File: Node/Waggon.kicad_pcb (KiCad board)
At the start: 2 copper layers, 34.3 x 74.9 mm, 40 parts, among them J1 Screw_Terminal_01x05, J10 Conn_01x01, J11 Conn_01x01, J12 Conn_01x01, J13 Conn_01x01, J14 Conn_01x01, J15 Conn_01x01, J16 Conn_01x01, J17 Conn_01x01, J18 Conn_01x01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

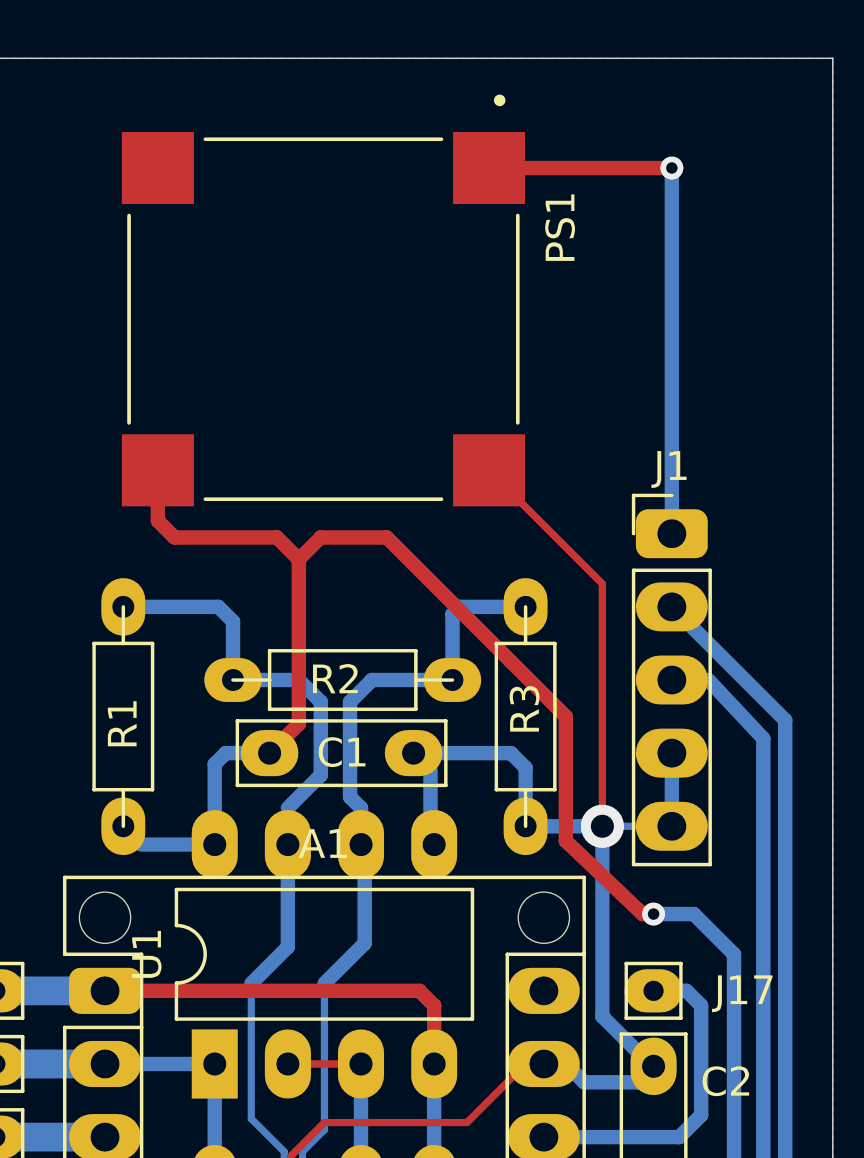
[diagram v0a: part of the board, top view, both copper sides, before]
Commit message: Adding KiCAD Footprints
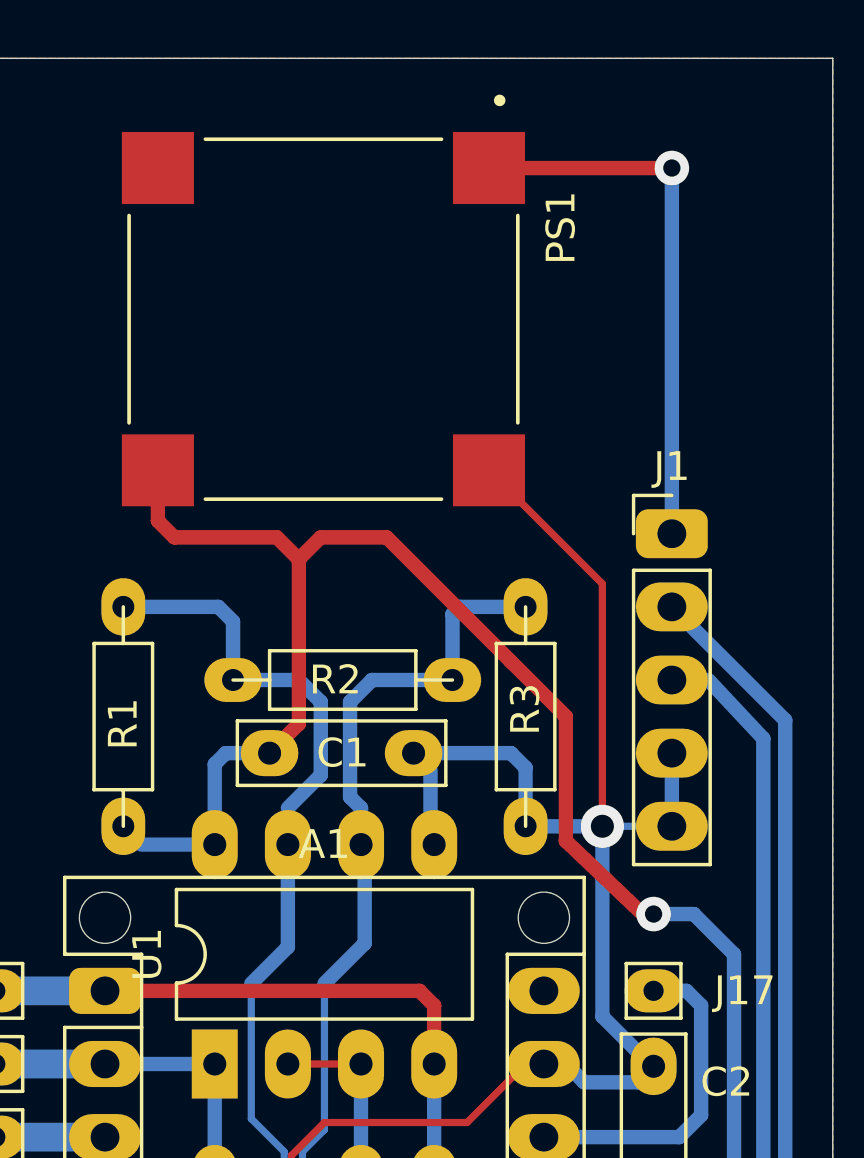
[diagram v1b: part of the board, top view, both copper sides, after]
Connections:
- A1 pad 30: Net-(A1-Pad30) -> unconnected-(A1-Pad30)
- PS1 pad 4: Net-(PS1-Pad4) -> unconnected-(PS1-Pad4)
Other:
- net class Default removed

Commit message: Updating Descriptions
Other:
- board text added: "+9..36V"
- board text added: "/RESET"
- board text added: "3V3"
- board text added: "A0"
- board text added: "A1"
- board text added: "A2"
- board text added: "A3"
- board text added: "A4"
- board text added: "A5"
- board text added: "A6"
- board text added: "A7"
- board text added: "ARef"
- board text added: "D10"
- board text added: "D13 / SCK / Built-In-LED"
- board text added: "D2"
- board text added: "D3"
- board text added: "D4"
- board text added: "D5"
- board text added: "D6"
- board text added: "D7"
- board text added: "D8"
- board text added: "D9"
- board text added: "GND"
- board text added: "LEDs in wagon DK: VU-Meter rt D2 ge D3 ge D4 gn D5 gn D7 gn D8 gn D9 gn D10 gn D13 LED top gn A7"
- board text added: "MISO / D12"
- board text added: "MOSI / D11"
- board text added: "PortA.0"
- board text added: "PortA.1"
- board text added: "PortA.2"
- board text added: "PortA.3"
- board text added: "PortA.4"
- board text added: "PortA.5"
- board text added: "PortA.6"
- board text added: "PortA.7"
- board text added: "PortB.0"
- board text added: "PortB.1"
- board text added: "PortB.2"
- board text added: "PortB.3"
- board text added: "PortB.4"
- board text added: "PortB.5"
- board text added: "PortB.6"
- board text added: "PortB.7"
- board text added: "RX1"
- board text added: "SCL / A"
- board text added: "SDA / B"
- board text added: "TX1"
- board text added: "black"
- board text added: "blue"
- board text added: "green"
- board text added: "magnetig connector"
- board text added: "plastic connector"
- board text added: "red"
- board text added: "white"
- board text added: "yellow"
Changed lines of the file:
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@@
   (gr_line (start 187.96 69.85) (end 222.25 69.85) (layer "Edge.Cuts") (width 0.05))
   (gr_line (start 222.25 144.78) (end 187.96 144.78) (layer "Edge.Cuts") (width 0.05))
+  (gr_text "/RESET" (at 226.314 102.108) (layer "F.SilkS")
+    (effects (font (size 1 1) (thickness 0.15)))
+  )
+  (gr_text "D10" (at 184.404 132.588) (layer "F.SilkS")
+    (effects (font (size 1 1) (thickness 0.15)))
+  )
+  (gr_text "D5" (at 185.039 119.888) (layer "F.SilkS")
+    (effects (font (size 1 1) (thickness 0.15)))
+  )
+  (gr_text "A5" (at 225.044 117.348) (layer "F.SilkS")
+    (effects (font (size 1 1) (thickness 0.15)))
+  )
+  (gr_text "A2" (at 225.044 124.968) (layer "F.SilkS")
+    (effects (font (size 1 1) (thickness 0.15)))
+  )
+  (gr_text "PortA.1" (at 177.419 114.808) (layer "F.SilkS")
+    (effects (font (size 1 1) (thickness 0.15)))
+  )
+  (gr_text "PortA.6" (at 177.419 127.508) (layer "F.SilkS")
+    (effects (font (size 1 1) (thickness 0.15)))
+  )
+  (gr_text "MISO / D12 " (at 181.864 137.668) (layer "F.SilkS")
+    (effects (font (size 1 1) (thickness 0.15)))
+  )
+  (gr_text "MOSI / D11" (at 181.229 135.128) (layer "F.SilkS")
+    (effects (font (size 1 1) (thickness 0.15)))
+  )
+  (gr_text "LEDs in wagon DK:\nVU-Meter\n	rt	D2\n	ge	D3\n	ge	D4\n	gn	D5\n	gn	D7\n	gn	D8\n	gn	D9\n	gn	D10\n	gn	D13\nLED top\n	gn	A7" (at 142.494 79.883) (layer "F.SilkS")
+    (effects (font (size 1 1) (thickness 0.15)) (justify left))
+  )
+  (gr_text "PortA.3" (at 177.419 119.888) (layer "F.SilkS")
+    (effects (font (size 1 1) (thickness 0.15)))
+  )
+  (gr_text "GND" (at 225.044 96.393) (layer "F.SilkS")
+    (effects (font (size 1 1) (thickness 0.15)))
+  )
+  (gr_text "ARef" (at 225.679 132.588) (layer "F.SilkS")
+    (effects (font (size 1 1) (thickness 0.15)))
+  )
+  (gr_text "D4" (at 185.039 117.348) (layer "F.SilkS")
+    (effects (font (size 1 1) (thickness 0.15)))
+  )
+  (gr_text "black" (at 248.539 93.853) (layer "F.SilkS")
+    (effects (font (size 1 1) (thickness 0.15)))
+  )
+  (gr_text "SCL / A" (at 226.314 91.313) (layer "F.SilkS")
+    (effects (font (size 1 1) (thickness 0.15)))
+  )
+  (gr_text "A0" (at 225.044 130.048) (layer "F.SilkS")
+    (effects (font (size 1 1) (thickness 0.15)))
+  )
+  (gr_text "D2" (at 185.039 112.268) (layer "F.SilkS")
+    (effects (font (size 1 1) (thickness 0.15)))
+  )
+  (gr_text "PortA.2" (at 177.419 117.348) (layer "F.SilkS")
+    (effects (font (size 1 1) (thickness 0.15)))
+  )
+  (gr_text "PortB.2" (at 171.069 137.668) (layer "F.SilkS")
+    (effects (font (size 1 1) (thickness 0.15)))
+  )
+  (gr_text "D13 / SCK / Built-In-LED" (at 234.569 137.668) (layer "F.SilkS")
+    (effects (font (size 1 1) (thickness 0.15)))
+  )
+  (gr_text "SDA / B" (at 226.314 88.773) (layer "F.SilkS")
+    (effects (font (size 1 1) (thickness 0.15)))
+  )
+  (gr_text "D8" (at 185.039 127.508) (layer "F.SilkS")
+    (effects (font (size 1 1) (thickness 0.15)))
+  )
+  (gr_text "plastic\nconnector" (at 246.634 81.788) (layer "F.SilkS")
+    (effects (font (size 1 1) (thickness 0.15)) (justify left))
+  )
+  (gr_text "D6" (at 185.039 122.428) (layer "F.SilkS")
+    (effects (font (size 1 1) (thickness 0.15)))
+  )
+  (gr_text "PortB.1" (at 171.069 135.128) (layer "F.SilkS")
+    (effects (font (size 1 1) (thickness 0.15)))
+  )
+  (gr_text "yellow" (at 236.474 88.773) (layer "F.SilkS")
+    (effects (font (size 1 1) (thickness 0.15)))
+  )
+  (gr_text "PortB.4" (at 233.934 130.048) (layer "F.SilkS")
+    (effects (font (size 1 1) (thickness 0.15)))
+  )
+  (gr_text "PortA.4" (at 177.419 122.428) (layer "F.SilkS")
+    (effects (font (size 1 1) (thickness 0.15)))
+  )
+  (gr_text "A1" (at 225.044 127.508) (layer "F.SilkS")
+    (effects (font (size 1 1) (thickness 0.15)))
+  )
+  (gr_text "PortB.7" (at 233.934 122.428) (layer "F.SilkS")
+    (effects (font (size 1 1) (thickness 0.15)))
+  )
+  (gr_text "PortA.5" (at 177.419 124.968) (layer "F.SilkS")
+    (effects (font (size 1 1) (thickness 0.15)))
+  )
+  (gr_text "D7" (at 185.039 124.968) (layer "F.SilkS")
+    (effects (font (size 1 1) (thickness 0.15)))
+  )
+  (gr_text "PortB.0" (at 171.069 132.588) (layer "F.SilkS")
+    (effects (font (size 1 1) (thickness 0.15)))
+  )
+  (gr_text "green" (at 248.539 88.773) (layer "F.SilkS")
+    (effects (font (size 1 1) (thickness 0.15)))
+  )
+  (gr_text "magnetig\nconnector" (at 233.934 81.788) (layer "F.SilkS")
+    (effects (font (size 1 1) (thickness 0.15)) (justify left))
+  )
+  (gr_text "PortA.0" (at 177.419 112.268) (layer "F.SilkS")
+    (effects (font (size 1 1) (thickness 0.15)))
+  )
+  (gr_text "PortA.7" (at 177.419 130.048) (layer "F.SilkS")
+    (effects (font (size 1 1) (thickness 0.15)))
+  )
+  (gr_text "A3" (at 225.044 122.428) (layer "F.SilkS")
+    (effects (font (size 1 1) (thickness 0.15)))
+  )
+  (gr_text "+9..36V" (at 225.679 86.233) (layer "F.SilkS")
+    (effects (font (size 1 1) (thickness 0.15)))
+  )
+  (gr_text "PortB.3" (at 250.444 137.668) (layer "F.SilkS")
+    (effects (font (size 1 1) (thickness 0.15)))
+  )
+  (gr_text "blue" (at 247.904 91.313) (layer "F.SilkS")
+    (effects (font (size 1 1) (thickness 0.15)))
+  )
+  (gr_text "/RESET" (at 183.769 107.188) (layer "F.SilkS")
+    (effects (font (size 1 1) (thickness 0.15)))
+  )
+  (gr_text "white" (at 235.839 91.313) (layer "F.SilkS")
+    (effects (font (size 1 1) (thickness 0.15)))
+  )
+  (gr_text "PortB.5" (at 233.934 127.508) (layer "F.SilkS")
+    (effects (font (size 1 1) (thickness 0.15)))
+  )
+  (gr_text "A4" (at 225.044 119.888) (layer "F.SilkS")
+    (effects (font (size 1 1) (thickness 0.15)))
+  )
+  (gr_text "D3" (at 185.039 114.808) (layer "F.SilkS")
+    (effects (font (size 1 1) (thickness 0.15)))
+  )
+  (gr_text "3V3" (at 225.679 135.128) (layer "F.SilkS")
+    (effects (font (size 1 1) (thickness 0.15)))
+  )
+  (gr_text "TX1" (at 185.039 102.108) (layer "F.SilkS")
+    (effects (font (size 1 1) (thickness 0.15)))
+  )
+  (gr_text "RX1" (at 185.039 104.648) (layer "F.SilkS")
+    (effects (font (size 1 1) (thickness 0.15)))
+  )
+  (gr_text "A6" (at 225.044 114.808) (layer "F.SilkS")
+    (effects (font (size 1 1) (thickness 0.15)))
+  )
+  (gr_text "red" (at 235.204 86.233) (layer "F.SilkS")
+    (effects (font (size 1 1) (thickness 0.15)))
+  )
+  (gr_text "red" (at 247.904 86.233) (layer "F.SilkS")
+    (effects (font (size 1 1) (thickness 0.15)))
+  )
+  (gr_text "A7" (at 225.044 112.268) (layer "F.SilkS")
+    (effects (font (size 1 1) (thickness 0.15)))
+  )
+  (gr_text "D9" (at 185.039 130.048) (layer "F.SilkS")
+    (effects (font (size 1 1) (thickness 0.15)))
+  )
+  (gr_text "GND" (at 225.044 93.853) (layer "F.SilkS")
+    (effects (font (size 1 1) (thickness 0.15)))
+  )
+  (gr_text "black" (at 235.839 93.853) (layer "F.SilkS")
+    (effects (font (size 1 1) (thickness 0.15)))
+  )
+  (gr_text "PortB.6" (at 233.934 124.968) (layer "F.SilkS")
+    (effects (font (size 1 1) (thickness 0.15)))
+  )
   (segment (start 207.899 102.235) (end 208.407 102.743) (width 0.5) (layer "F.Cu") (net 1))
   (segment (start 208.407 102.743) (end 208.407 104.775) (width 0.5) (layer "F.Cu") (net 1))
